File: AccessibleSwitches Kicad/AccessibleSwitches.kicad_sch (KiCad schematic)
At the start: 3 parts, among them J1 Conn_01x02_Socket, SW1 D2FS-F-N

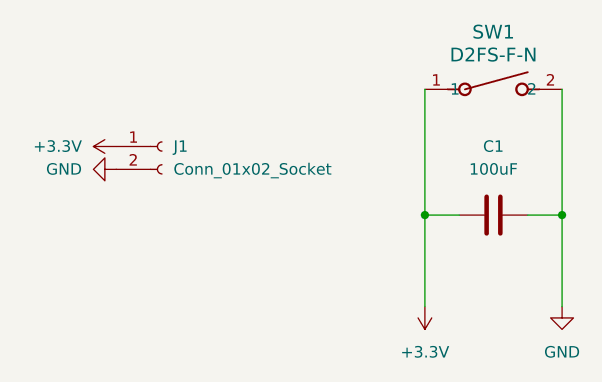
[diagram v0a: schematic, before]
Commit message: SMD debouncing cap added
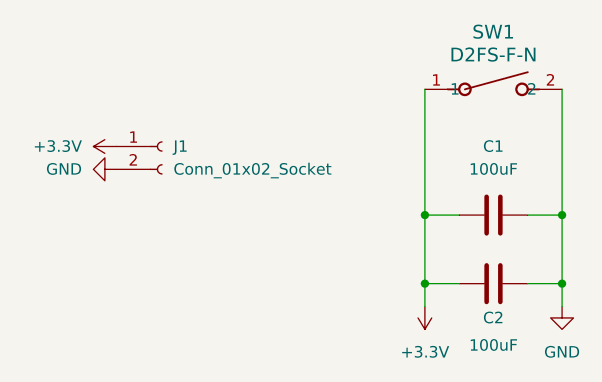
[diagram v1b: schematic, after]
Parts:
- added C2: 100uF, Capacitor_THT:CP_Radial_D6.3mm_P2.50mm, symbol Device:C
- C1: footprint Capacitor_THT:CP_Radial_D6.3mm_P2.50mm -> Capacitor_SMD:C_0603_1608Metric_Pad1.08x0.95mm_HandSolder
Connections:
- net +3.3V: now also C2.1
- net GND: now also C2.2
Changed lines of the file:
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@@
 	(paper "A4")
+	(junction
+		(at 180.34 96.52)
+		(diameter 0)
+		(color 0 0 0 0)
+	)
 	(junction
 		(at 180.34 88.9)
@@
 	)
 	(junction
+		(at 165.1 96.52)
+		(diameter 0)
+		(color 0 0 0 0)
+	)
+	(junction
 		(at 165.1 88.9)
 		(diameter 0)
@@
 	(wire
 		(pts
+			(xy 180.34 96.52) (xy 180.34 88.9)
+		)
+		(stroke
+			(width 0)
+			(type default)
+		)
+	)
+	(wire
+		(pts
+			(xy 165.1 96.52) (xy 165.1 99.06)
+		)
+		(stroke
+			(width 0)
+			(type default)
+		)
+	)
+	(wire
+		(pts
 			(xy 165.1 88.9) (xy 168.91 88.9)
 		)
@@
 	(wire
 		(pts
-			(xy 165.1 88.9) (xy 165.1 99.06)
-		)
-		(stroke
-			(width 0)
-			(type default)
-		)
-	)
-	(wire
-		(pts
-			(xy 180.34 99.06) (xy 180.34 88.9)
+			(xy 165.1 88.9) (xy 165.1 96.52)
+		)
+		(stroke
+			(width 0)
+			(type default)
+		)
+	)
+	(wire
+		(pts
+			(xy 165.1 96.52) (xy 168.91 96.52)
+		)
+		(stroke
+			(width 0)
+			(type default)
+		)
+	)
+	(wire
+		(pts
+			(xy 180.34 99.06) (xy 180.34 96.52)
 		)
 		(stroke
@@
 		(pts
 			(xy 180.34 74.93) (xy 180.34 88.9)
+		)
+		(stroke
+			(width 0)
+			(type default)
+		)
+	)
+	(wire
+		(pts
+			(xy 176.53 96.52) (xy 180.34 96.52)
 		)
 		(stroke
@@
 			)
 		)
-		(property "Footprint" "Capacitor_THT:CP_Radial_D6.3mm_P2.50mm"
+		(property "Footprint" "Capacitor_SMD:C_0603_1608Metric_Pad1.08x0.95mm_HandSolder"
 			(at 176.53 87.9348 0)
 			(effects
@@
 					(unit 1)
 				)
+			)
+		)
+	)
+	(symbol
+		(lib_id "Device:C")
+		(at 172.72 96.52 90)
+		(unit 1)
+		(exclude_from_sim no)
+		(in_bom yes)
+		(on_board yes)
+		(dnp no)
+		(property "Reference" "C2"
+			(at 172.72 100.33 90)
+			(effects
+				(font
+					(size 1.27 1.27)
+				)
+			)
+		)
+		(property "Value" "100uF"
+			(at 172.72 103.378 90)
+			(effects
+				(font
+					(size 1.27 1.27)
+				)
+			)
+		)
+		(property "Footprint" "Capacitor_THT:CP_Radial_D6.3mm_P2.50mm"
+			(at 176.53 95.5548 0)
+			(effects
+				(font
+					(size 1.27 1.27)
+				)
+				(hide yes)
+			)
+		)
+		(property "Datasheet" "~"
+			(at 172.72 96.52 0)
+			(effects
+				(font
+					(size 1.27 1.27)
+				)
+				(hide yes)
+			)
+		)
+		(property "Description" "Unpolarized capacitor"
+			(at 172.72 96.52 0)
+			(effects
+				(font
+					(size 1.27 1.27)
+				)
+				(hide yes)
+			)
+		)
+		(pin "1"
+		)
+		(pin "2"
+		)
+		(instances
+			(project "AccessibleSwitches"
+				(path "/ba6d9f2d-ef3e-4e6a-a138-610a5f2bdda8"
+					(reference "C2")
+					(unit 1)
+				)
